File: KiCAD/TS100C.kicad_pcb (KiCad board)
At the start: 4 copper layers, 84 x 10 mm, 52 parts, among them J1 USB_C, J2 OLED_64x32, J3 A, J4 B, J5 DNP, P1 TC2030-CTX, Q1 SS8050, Q2 DMP3017SFG, SW1 key1, SW2 key2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

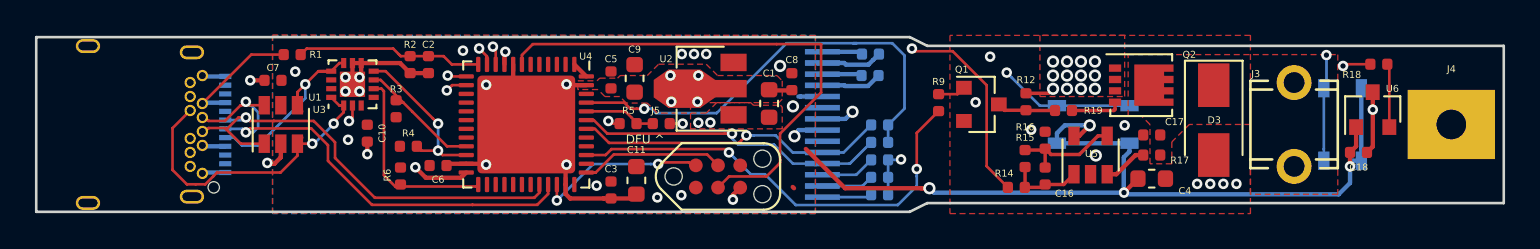
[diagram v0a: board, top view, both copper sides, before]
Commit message: updated PCB+schematic to STUSB4500
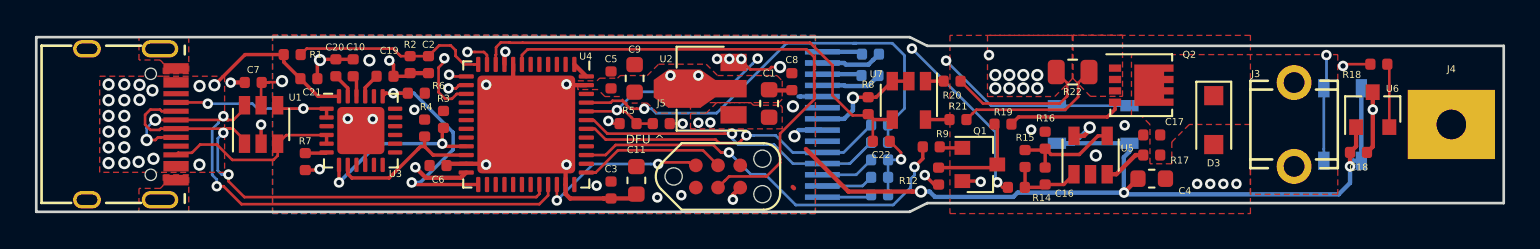
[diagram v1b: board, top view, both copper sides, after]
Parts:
- added C19: 0.1μF, Capacitor_SMD:C_0402_1005Metric, F.Cu at (100.0, 82.2)
- added C20: 0.1μF, Capacitor_SMD:C_0402_1005Metric, F.Cu at (97.2, 81.8)
- added C21: 0.1μF, Capacitor_SMD:C_0402_1005Metric, F.Cu at (95.6, 82.4)
- added C22: 0.1μF, Capacitor_SMD:C_0402_1005Metric, F.Cu at (128.4, 86.0)
- added R20: 33, Resistor_SMD:R_0402_1005Metric, F.Cu at (132.4, 82.5)
- added R21: 33, Resistor_SMD:R_0402_1005Metric, F.Cu at (132.8, 84.7)
- added R22: 10m, Resistor_SMD:R_0805_2012Metric, F.Cu at (139.3, 82.0)
- added R7: 2kΩ, Resistor_SMD:R_0402_1005Metric, F.Cu at (95.4, 87.1)
- added R8: 2k, Resistor_SMD:R_0402_1005Metric, F.Cu at (127.6, 83.9)
- added U7: SI8540, Package_TO_SOT_SMD:SOT-23-5, F.Cu at (129.9, 83.6)
- D3: footprint Diode_SMD:D_SMA -> Diode_SMD:D_SOD-123F
- J1: value USB_C -> USB_C_Receptacle_USB2.0; footprint Connector_USB:USB_C_Receptacle_Amphenol_12401548E4-2A -> otter:USB-C 16Pin; moved to F.Cu
- U3: value FUSB302BMPX -> STUSB4500; footprint Package_DFN_QFN:WQFN-14-1EP_2.5x2.5mm_P0.5mm_EP1.45x1.45mm -> Package_DFN_QFN:QFN-24-1EP_4x4mm_P0.5mm_EP2.7x2.7mm
- moved R12 6.57 mm to (131.7, 88.0), turned to 90 degrees
- moved R6 4.83 mm to (101.8, 83.2), turned to 0 degrees
- moved C10 3.83 mm to (98.1, 81.8), turned to 90 degrees
- moved R19 3.55 mm to (135.3, 85.0)
- moved Q1 3.44 mm to (134.0, 87.3)
- moved R3 2.78 mm to (103.3, 84.7), turned to 90 degrees
- moved U3 2.69 mm to (98.6, 85.3), turned to 0 degrees
- moved R9 2.56 mm to (131.2, 86.3), turned to 0 degrees
- moved J1 2.20 mm to (88.0, 85.0), turned to 270 degrees
- moved R4 1.40 mm to (102.2, 85.2), turned to 90 degrees
- moved C7 1.14 mm to (92.4, 82.6)
- moved U1 1.13 mm to (92.9, 85.0)
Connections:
- J5 pad 1: Net-(J5-Pad1) -> SW1
- Q2 pad 1: VBUS -> Net-(Q2-Pad1)
- Q2 pad 2: VBUS -> Net-(Q2-Pad1)
- Q2 pad 3: VBUS -> Net-(Q2-Pad1)
- R5 pad 2: Net-(J5-Pad1) -> SW1
- SW1 pad 2: Net-(SW1-Pad2) -> SW1
- U3 pad 1: CC2 -> CC1
- U3 pad 10: CC1 -> GND
- U3 pad 11: CC1 -> Net-(U3-Pad11)
- U3 pad 14: CC2 -> Net-(U3-Pad14)
- U3 pad 15: GND -> Net-(U3-Pad15)
- U3 pad 2: VBUS -> CC1
- U3 pad 3: +3V3 -> Net-(U3-Pad3)
- U3 pad 4: +3V3 -> CC2
- U3 pad 5: INT_N -> CC2
- U3 pad 6: SCL -> Net-(R7-Pad2)
- U3 pad 7: SDA -> SCL
- U3 pad 8: GND -> SDA
- U3 pad 9: GND -> Net-(U3-Pad9)
- U4 pad 10: TREF -> IIN
- U4 pad 13: Net-(SW1-Pad2) -> SW1
- U4 pad 15: Net-(U4-Pad15) -> TREF
- U4 pad 44: Net-(J5-Pad1) -> SW1
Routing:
- net SW1: track 0.00 -> 56.2 mm, vias 0 -> 4
- net Net-(SW1-Pad2): track 41.7 -> 0.00 mm, vias 2 -> 0
- net IIN: track 0.00 -> 28.4 mm
- net Net-(Q2-Pad1): track 0.00 -> 8.61 mm
- net VBUS: track 11.1 -> 18.7 mm, vias 15 -> 31
- net CC2: track 17.7 -> 10.7 mm, vias 2 -> 0
- net +3V3: track 62.2 -> 68.5 mm
- net USB_P: track 28.6 -> 33.7 mm, vias 2 -> 4
- net USB_N: track 26.5 -> 31.4 mm, vias 1 -> 2
- net GND: track 51.7 -> 56.5 mm, vias 28 -> 26
- net Net-(J5-Pad1): track 4.20 -> 0.00 mm
- net Net-(Q2-Pad4): track 2.90 -> 6.69 mm
- net Net-(SW2-Pad2): track 62.5 -> 59.0 mm
- net TREF: track 55.5 -> 58.6 mm
- net SCL: track 7.34 -> 10.4 mm, vias 0 -> 2
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- added copper zone on F.Cu, net Net-(Q2-Pad1)
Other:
- net class Default: trace_width 0.25 -> 0.154

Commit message: added silkscreen
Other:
- board text added: "Design by: JanHenrik"
- board text added: "Otter-Iron"
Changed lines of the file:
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@@
   (general
     (thickness 1.6)
-    (drawings 9)
+    (drawings 11)
     (tracks 617)
     (zones 0)
@@
       (usegerberadvancedattributes false)
       (creategerberjobfile false)
-      (excludeedgelayer true)
+      (excludeedgelayer false)
       (linewidth 0.100000)
       (plotframeref false)
@@
       (drillshape 0)
       (scaleselection 1)
-      (outputdirectory ""))
+      (outputdirectory "gerber/"))
   )
   (net 0 "")
@@
     (tags capacitor)
     (attr smd)
-    (fp_text reference C22 (at -0.01 0.78) (layer F.SilkS)
+    (fp_text reference C22 (at 1.44 -0.29) (layer F.SilkS)
       (effects (font (size 0.4 0.4) (thickness 0.1)))
     )
@@
     )
   )
+  (gr_text "Design by:\nJanHenrik" (at 125.84 88.5) (layer F.SilkS)
+    (effects (font (size 0.6 0.6) (thickness 0.1)))
+  )
+  (gr_text Otter-Iron (at 125.84 86.99) (layer F.SilkS)
+    (effects (font (size 0.8 0.8) (thickness 0.1)))
+  )
   (gr_text "DFU ^" (at 114.85 85.85) (layer F.SilkS)

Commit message: updated pcb
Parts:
- added R23: 2kΩ, Resistor_SMD:R_0402_1005Metric, F.Cu at (92.8, 87.8)
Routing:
- net Net-(R23-Pad1): track 0.00 -> 13.4 mm, vias 0 -> 2
- net VBUS: track 18.7 -> 21.9 mm
- net INT_N: track 13.9 -> 13.1 mm

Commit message: updated hardware
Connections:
- U3 pad 12: Net-(U3-Pad12) -> GND
- U3 pad 13: Net-(U3-Pad13) -> GND
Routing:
- net GND: track 56.5 -> 59.7 mm
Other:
- rule pad_to_mask_clearance: 0.154 -> 0.1
- rule solder_mask_min_width: 0.25 -> 0.154

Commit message: added todos
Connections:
- U4 pad 29: Net-(U4-Pad29) -> PWM
- U4 pad 39: PWM -> Net-(U4-Pad39)

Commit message: fixed bom
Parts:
- C1: value 1.0μF 25V -> 1μF 25V
- C11, C9: value 1μF -> 1μF 25V
- C16: value 0.1uF -> TBD (18p)
- C17: value 0.1μF -> TBD (100n)
- C4: value 2.2μF -> 1μF 25V
- J1: moved to B.Cu
- R10, R13, R5, R8, R9: value 2k -> 2k37
- R12: value 10k -> 2k37
- R14, R18: value 1k -> 2k37
- R23, R3, R4, R6, R7: value 2kΩ -> 2k37
- moved R5 0.84 mm to (113.2, 84.5), turned to 270 degrees
- moved J5 0.74 mm to (115.0, 85.0)
- turned J1 to 90 degrees
- turned SW1 to 90 degrees
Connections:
- J5 pad 1: SW1 -> Net-(J5-Pad1)
- R10 pad 2: OLED_PULLUP -> +3V3
- R13 pad 2: OLED_PULLUP -> +3V3
- R5 pad 2: SW1 -> Net-(J5-Pad1)
- SW1 pad 2: SW1 -> Net-(SW1-Pad2)
- U4 pad 13: SW1 -> Net-(SW1-Pad2)
- U4 pad 44: SW1 -> Net-(J5-Pad1)
- U4 pad 45: OLED_PULLUP -> Net-(U4-Pad45)
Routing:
- net SW1: track 56.2 -> 0.00 mm, vias 4 -> 0
- net Net-(SW1-Pad2): track 0.00 -> 43.2 mm, vias 0 -> 2
- net OLED_PULLUP: track 26.1 -> 0.00 mm, vias 1 -> 0
- net PWM: track 23.3 -> 34.9 mm, vias 2 -> 4
- net +3V3: track 68.1 -> 73.7 mm
- net Net-(J5-Pad1): track 0.00 -> 3.35 mm
- net CC1: track 10.8 -> 12.8 mm, vias 2 -> 3
- net USB_P: track 33.7 -> 32.1 mm, vias 4 -> 2
- net USB_N: track 31.4 -> 29.9 mm, vias 2 -> 3
- net CC2: track 10.3 -> 10.9 mm, vias 0 -> 1
- net GND: track 59.7 -> 60.1 mm, vias 26 -> 25
- added copper zone on B.Cu, net GND
- added copper zone on B.Cu, net VBUS
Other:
- rule trace_min: 0.154 -> 0.1
- rule via_min_drill: 0.3 -> 0.2

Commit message: optimized values
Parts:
- C12, C13, C14, C15: value 1uF -> 1μF 25V
- C16: value TBD (18p) -> 18p
- C17: value TBD (100n) -> DNP
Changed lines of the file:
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@@
       (effects (font (size 0.4 0.4) (thickness 0.1)))
     )
-    (fp_text value "TBD (18p)" (at 0 1.17 270) (layer F.Fab)
+    (fp_text value 18p (at 0 1.17 270) (layer F.Fab)
       (effects (font (size 1 1) (thickness 0.15)))
     )
@@
       (effects (font (size 0.4 0.4) (thickness 0.1)))
     )
-    (fp_text value "TBD (100n)" (at 0 1.17) (layer F.Fab)
+    (fp_text value DNP (at 0 1.17) (layer F.Fab)
       (effects (font (size 1 1) (thickness 0.15)))
     )
@@
       (effects (font (size 0.4 0.4) (thickness 0.1)) (justify mirror))
     )
-    (fp_text value 1uF (at 0 -1.17) (layer B.Fab)
+    (fp_text value "1μF 25V" (at 0 -1.17) (layer B.Fab)
       (effects (font (size 1 1) (thickness 0.15)) (justify mirror))
     )
@@
       (effects (font (size 0.4 0.4) (thickness 0.1)) (justify mirror))
     )
-    (fp_text value 1uF (at 0 -1.17) (layer B.Fab)
+    (fp_text value "1μF 25V" (at 0 -1.17) (layer B.Fab)
       (effects (font (size 1 1) (thickness 0.15)) (justify mirror))
     )
@@
       (effects (font (size 0.4 0.4) (thickness 0.1)) (justify mirror))
     )
-    (fp_text value 1uF (at 0 -1.17 180) (layer B.Fab)
+    (fp_text value "1μF 25V" (at 0 -1.17 180) (layer B.Fab)
       (effects (font (size 1 1) (thickness 0.15)) (justify mirror))
     )
@@
       (effects (font (size 0.4 0.4) (thickness 0.1)) (justify mirror))
     )
-    (fp_text value 1uF (at 0 -1.17) (layer B.Fab)
+    (fp_text value "1μF 25V" (at 0 -1.17) (layer B.Fab)
       (effects (font (size 1 1) (thickness 0.15)) (justify mirror))
     )

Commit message: fixed STM
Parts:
- U4: value STM32F072C8Ux -> STM32F072CBUx
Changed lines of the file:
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@@
-(kicad_pcb (version 20171130) (host pcbnew 5.0.1)
+(kicad_pcb (version 20171130) (host pcbnew 5.1.4+dfsg1-1)
   (general
     (thickness 1.6)
@@
     (zone_45_only no)
     (trace_min 0.1)
-    (segment_width 0.2)
-    (edge_width 0.15)
     (via_size 0.7)
     (via_drill 0.4)
@@
     (uvia_min_size 0.2)
     (uvia_min_drill 0.1)
+    (edge_width 0.15)
+    (segment_width 0.2)
     (pcb_text_width 0.3)
     (pcb_text_size 1.5 1.5)
@@
     (uvia_dia 0.3)
     (uvia_drill 0.1)
+    (diff_pair_width 0.154)
     (diff_pair_gap 0.25)
-    (diff_pair_width 0.154)
     (add_net +3V3)
     (add_net /OUT)
@@
       (effects (font (size 0.4 0.4) (thickness 0.1)))
     )
-    (fp_text value STM32F072C8Ux (at 0 4.82 270) (layer F.Fab)
-      (effects (font (size 1 1) (thickness 0.15)))
-    )
+    (fp_text value STM32F072CBUx (at 0 4.82 270) (layer F.Fab)
+      (effects (font (size 1 1) (thickness 0.15)))
+    )
